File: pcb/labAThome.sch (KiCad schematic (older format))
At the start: 57 parts, among them J1 BME280, J10 SRV2, J12 FA2, J13 Barrel_Jack_Switch, J14 FA3, J2 SRV1, J3 5V, J4 EXTENSION, J5 VPS, J9 FA1, K1 G5V-2, K2 G5V-2, K3 G5V-2, Q2 IRLZ44N, Q3 IRLZ44N, Q4 BC547, SW1 RED, SW2 GREEN, SW3 YELLOW, SW4 BLUE, SW5 WHITE, SW6 FAN, U1 HC-SR501, U2 24V->5V, U3 PDC004_Module, U4 ESP32_DEVKITC_COMPATIBLE, U5 LD06AJSA, U6 GY-302, U7 Display, U8 INMP441_Module

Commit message: SchematicsV3 as ordered at JLCPCB
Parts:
- removed D1: RED, LED_THT:LED_D5.0mm, symbol Device:LED
- removed D2: GREEN, LED_THT:LED_D5.0mm, symbol Device:LED
- removed D3: YELLOW, LED_THT:LED_D5.0mm, symbol Device:LED
- removed J1: BME280, Connector_PinHeader_2.54mm:PinHeader_1x06_P2.54mm_Vertical, symbol Connector:Conn_01x06_Male
- removed J14: FA3, Connector:FanPinHeader_1x03_P2.54mm_Vertical, symbol Connector_Generic:Conn_01x03
- removed J3: 5V, Connector_PinHeader_2.54mm:PinHeader_1x05_P2.54mm_Vertical, symbol Connector_Generic:Conn_01x05
- removed JP3: 3V3_5V, Jumper:SolderJumper-3_P2.0mm_Open_TrianglePad1.0x1.5mm_NumberLabels, symbol Jumper:SolderJumper_3_Open
- removed U1: HC-SR501, smopla:HC-SR501, symbol smopla:HC-SR501
- added C1: CP, Capacitor_THT:CP_Radial_Tantal_D5.0mm_P5.00mm, symbol Device:CP
- added D5: 1N4001, Diode_THT:D_DO-41_SOD81_P7.62mm_Horizontal, symbol Diode:1N4001
- added J1: BME280, Connector_PinHeader_2.54mm:PinHeader_1x04_P2.54mm_Vertical, symbol Connector:Conn_01x04_Male
- added J11, J7, J8: 1wire, Connector_JST:JST_PH_B3B-PH-K_1x03_P2.00mm_Vertical, symbol Connector_Generic:Conn_01x03
- added J3: 5V, Connector_PinHeader_2.54mm:PinHeader_1x04_P2.54mm_Vertical, symbol Connector:Conn_01x04_Male
- added J6: FAN3, Connector:FanPinHeader_1x03_P2.54mm_Vertical, symbol Connector_Generic:Conn_01x03
- added JP3: R3_BUZZ, Connector_PinSocket_2.54mm:PinSocket_1x03_P2.54mm_Vertical, symbol Jumper:Jumper_3_Open
- added JP4: 5V FAN1+2 24V, Connector_PinSocket_2.54mm:PinSocket_1x03_P2.54mm_Vertical, symbol Jumper:Jumper_3_Open
- added Q1: IRLZ44N, Package_TO_SOT_THT:TO-220-3_Horizontal_TabDown, symbol Device:Q_NMOS_GDS
- added U1: SR602, smopla:SR602, symbol smopla:SR602
- added U10: MAX3485_MODULE, smopla:MAX3485_MODULE, symbol smopla:MAX3485_MODULE
- added U11: AM312, smopla:AM312, symbol smopla:HC-SR501
- added U9: NEOPIXEL_STICK, smopla:NEOPIXEL_STICK, symbol smopla:NEOPIXEL_STICK
- added X1: FAN_6024, smopla:FAN_6024, symbol smopla:FAN_6024
- BZ1: footprint Buzzer_Beeper:Buzzer_12x9.5RM7.6 -> smopla:Buzzer_12x9.5RM6.6
- D8: footprint Diode_THT:D_DO-35_SOD27_P7.62mm_Horizontal -> Diode_THT:D_DO-35_SOD27_P2.54mm_Vertical_AnodeUp
- J12: value FA2 -> FAN2
- J9: value FA1 -> FAN1
- Q4: footprint Package_TO_SOT_THT:TO-92_Inline -> Package_TO_SOT_THT:TO-92_HandSolder
- R1, R13, R14, R15, R16, R2, R6: footprint Resistor_THT:R_Axial_DIN0207_L6.3mm_D2.5mm_P7.62mm_Horizontal -> Resistor_THT:R_Axial_DIN0207_L6.3mm_D2.5mm_P2.54mm_Vertical
- R3, R5: value 68R -> 1K; footprint Resistor_THT:R_Axial_DIN0207_L6.3mm_D2.5mm_P7.62mm_Horizontal -> Resistor_THT:R_Axial_DIN0207_L6.3mm_D2.5mm_P2.54mm_Vertical
- R4: value 68R -> 10K; footprint Resistor_THT:R_Axial_DIN0207_L6.3mm_D2.5mm_P7.62mm_Horizontal -> Resistor_THT:R_Axial_DIN0207_L6.3mm_D2.5mm_P2.54mm_Vertical
- SW6: value FAN -> FAN2; footprint smopla:MTS-102 -> smopla:SS12D00
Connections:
- net labels added: 1wire, FAN_SWITCH2, LCD_RES, LED_STRIP
- net labels removed: LED_GREEN, LED_RED, LED_YELLOW
- wire segments 71 -> 80
- no-connect marks 14 -> 16
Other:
- note added: "Gegenseitiger Ausschluss:\n- 1wire und Servo2\n- I2S und RS485\n- Relay 3 und Buzzer"
- note added: "Muss MOSI"
- note added: "PD->Mosfet"
- note added: "PU->SW"
- note removed: "Frei"
- note removed: "PULLED UP"
- note removed: "Soll LED"
- note removed: "Soll SW"
- note removed: "WPD Soll Mosfet"
- moved on the sheet: BZ1, D4, J10, J12, J2, J4, J5, J9, JP2, K1, Q2, Q3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

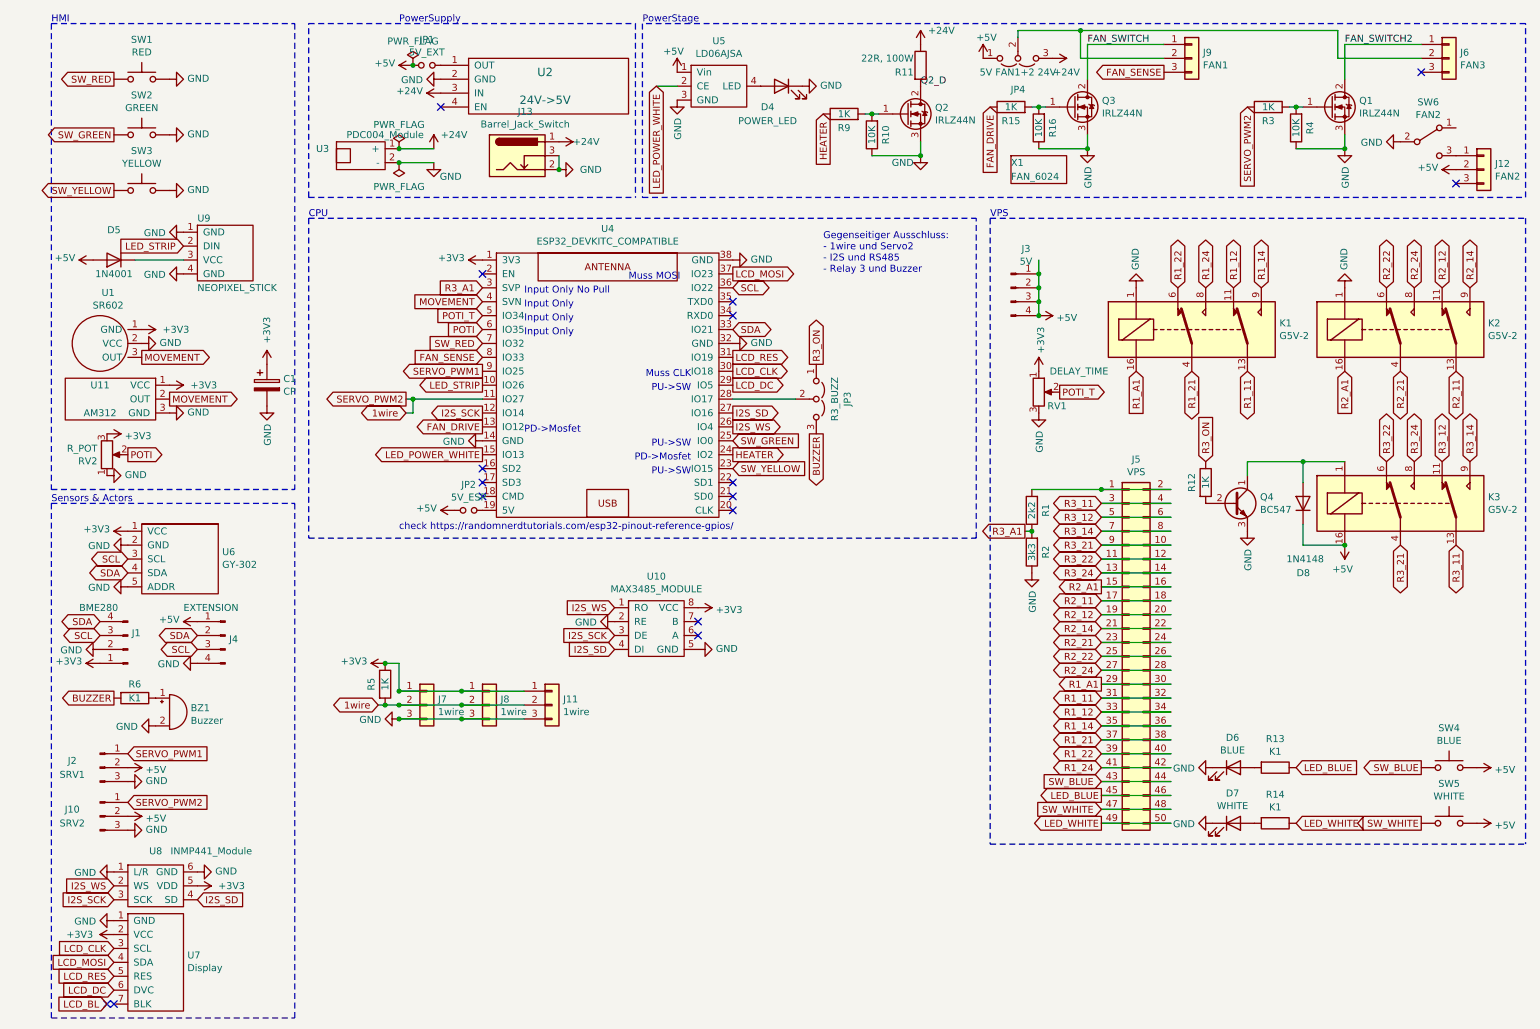
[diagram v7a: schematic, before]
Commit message: PCB  V4 as ordered at JLCPCB
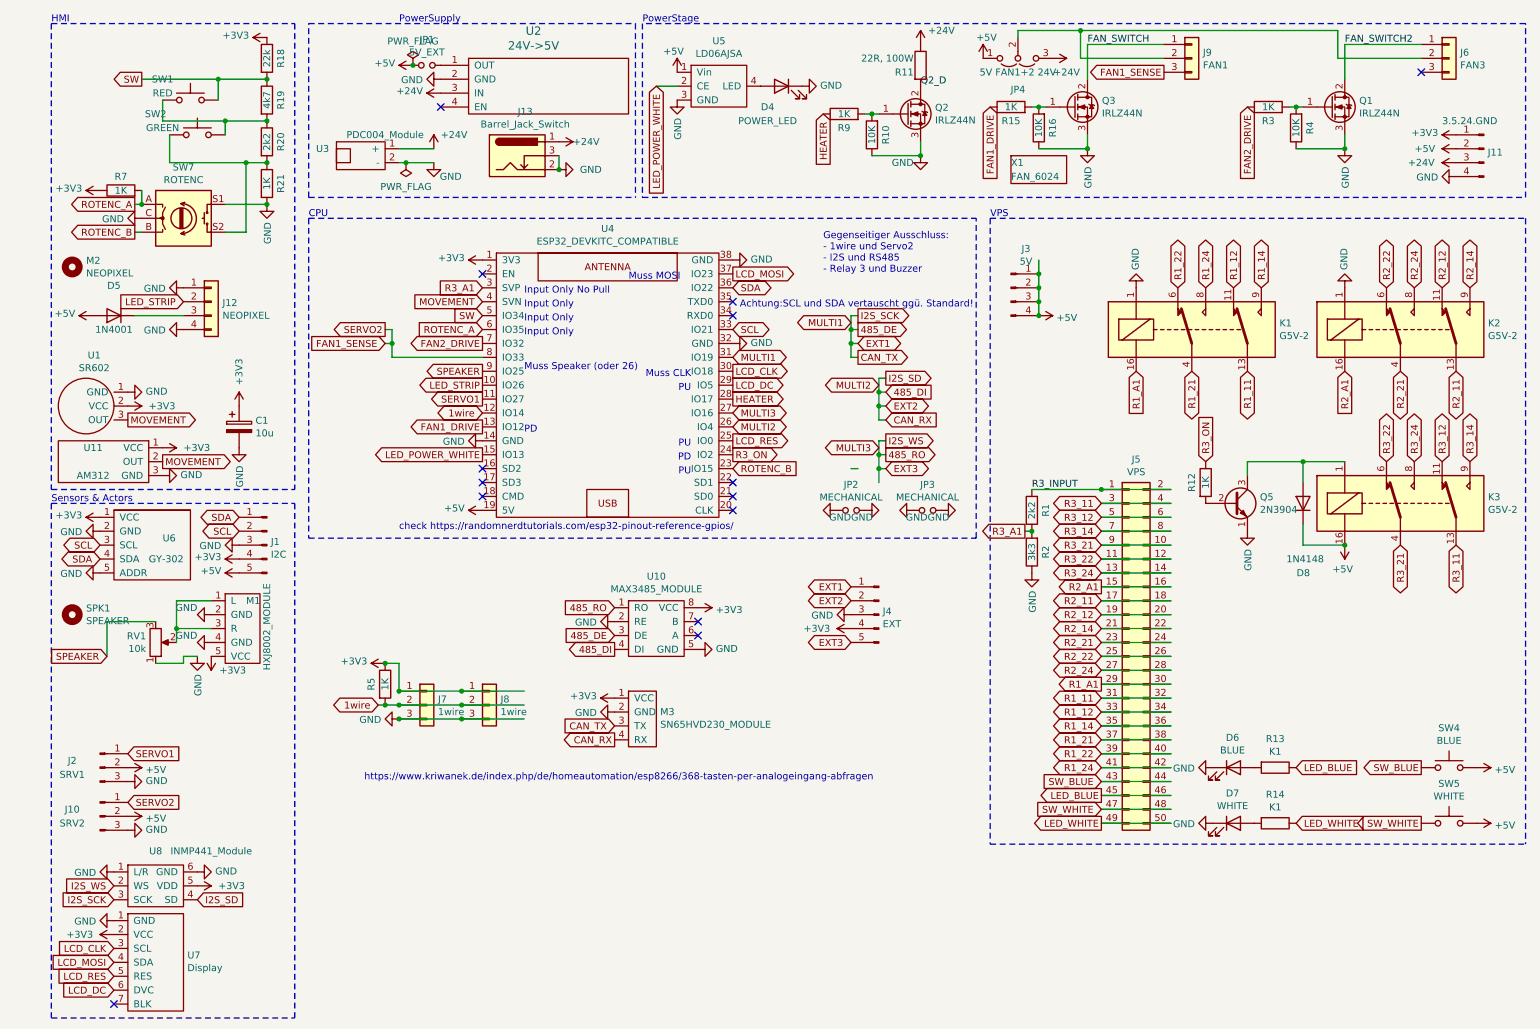
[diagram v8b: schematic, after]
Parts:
- removed BZ1: Buzzer, smopla:Buzzer_12x9.5RM6.6, symbol Device:Buzzer
- removed J1: BME280, Connector_PinHeader_2.54mm:PinHeader_1x04_P2.54mm_Vertical, symbol Connector:Conn_01x04_Male
- removed J11: 1wire, Connector_JST:JST_PH_B3B-PH-K_1x03_P2.00mm_Vertical, symbol Connector_Generic:Conn_01x03
- removed J12: FAN2, Connector:FanPinHeader_1x03_P2.54mm_Vertical, symbol Connector_Generic:Conn_01x03
- removed J4: EXTENSION, Connector_JST:JST_XH_B4B-XH-A_1x04_P2.50mm_Vertical, symbol Connector:Conn_01x04_Male
- removed JP3: R3_BUZZ, Connector_PinSocket_2.54mm:PinSocket_1x03_P2.54mm_Vertical, symbol Jumper:Jumper_3_Open
- removed Q4: BC547, Package_TO_SOT_THT:TO-92_HandSolder, symbol Transistor_BJT:BC547
- removed R6: K1, Resistor_THT:R_Axial_DIN0207_L6.3mm_D2.5mm_P2.54mm_Vertical, symbol Device:R
- removed RV2: R_POT, Potentiometer_THT:Potentiometer_Alpha_RD901F-40-00D_Single_Vertical, symbol Device:R_POT
- removed SW3: YELLOW, Button_Switch_THT:SW_PUSH-12mm, symbol Switch:SW_Push
- removed SW6: FAN2, smopla:SS12D00, symbol Switch:SW_SPDT
- removed U9: NEOPIXEL_STICK, smopla:NEOPIXEL_STICK, symbol smopla:NEOPIXEL_STICK
- added J1: I2C, Connector_JST:JST_XH_B5B-XH-AM_1x05_P2.50mm_Vertical, symbol Connector:Conn_01x05_Male
- added J11: 3.5.24.GND, Connector_JST:JST_XH_B4B-XH-A_1x04_P2.50mm_Vertical, symbol Connector:Conn_01x04_Male
- added J12: NEOPIXEL, Connector_PinSocket_2.54mm:PinSocket_1x04_P2.54mm_Vertical, symbol Connector_Generic:Conn_01x04
- added J4: EXT, Connector_JST:JST_XH_B5B-XH-AM_1x05_P2.50mm_Vertical, symbol Connector:Conn_01x05_Male
- added JP3: MECHANICAL, Connector_PinHeader_2.54mm:PinHeader_1x02_P2.54mm_Vertical, symbol Device:Jumper_NO_Small
- added M1: HXJ8002_MODULE, smopla:HXJ8002_MODULE_VERTICAL, symbol smopla:HXJ8002_MODULE
- added M2: NEOPIXEL, smopla:NEOPIXEL_STICK, symbol Mechanical:MountingHole
- added M3: SN65HVD230_MODULE, smopla:SN65HVD230_MODULE, symbol smopla:SN65HVD230_MODULE
- added Q5: 2N3904, Package_TO_SOT_THT:TO-92_HandSolder, symbol Transistor_BJT:2N3904
- added R18: 22k, Resistor_THT:R_Axial_DIN0207_L6.3mm_D2.5mm_P2.54mm_Vertical, symbol Device:R
- added R19: 4k7, Resistor_THT:R_Axial_DIN0207_L6.3mm_D2.5mm_P2.54mm_Vertical, symbol Device:R
- added R20: 2k2, Resistor_THT:R_Axial_DIN0207_L6.3mm_D2.5mm_P2.54mm_Vertical, symbol Device:R
- added R21, R7: 1K, Resistor_THT:R_Axial_DIN0207_L6.3mm_D2.5mm_P2.54mm_Vertical, symbol Device:R
- added SPK1: SPEAKER, smopla:SPEAKER_2415, symbol Mechanical:MountingHole
- added SW7: ROTENC, smopla:RotaryEncoder_Alps_EC11E-Switch_Vertical_H20mm, symbol Device:Rotary_Encoder_Switch
- C1: value CP -> 10u
- JP2: value 5V_ESP -> MECHANICAL
- R12, R9: footprint Resistor_THT:R_Axial_DIN0207_L6.3mm_D2.5mm_P7.62mm_Horizontal -> Resistor_THT:R_Axial_DIN0207_L6.3mm_D2.5mm_P2.54mm_Vertical
- RV1: value DELAY_TIME -> 10k; footprint Potentiometer_THT:Potentiometer_Bourns_3296W_Vertical -> Potentiometer_THT:Potentiometer_Runtron_RM-065_Vertical
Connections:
- net labels added: 485_DE, 485_DI, 485_RO, CAN_RX, CAN_TX, EXT1, EXT2, EXT3, FAN1_DRIVE, FAN1_SENSE, FAN2_DRIVE, MULTI1, MULTI2, MULTI3, R3_INPUT, ROTENC_A, ROTENC_B, SERVO1, SERVO2, SPEAKER, SW
- net labels removed: BUZZER, FAN_DRIVE, FAN_SENSE, LCD_BL, POTI, POTI_T, SERVO_PWM1, SERVO_PWM2, SW_GREEN, SW_RED, SW_YELLOW
- wire segments 80 -> 127
- no-connect marks 16 -> 14
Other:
- note added: "Achtung:SCL und SDA vertauscht ggü. Standard!"
- note added: "Muss Speaker (oder 26)"
- note added: "PD"
- note added: "PU"
- note added: "https://www.kriwanek.de/index.php/de/homeautomation/esp8266/368-tasten-per-analogeingang-abfragen"
- note removed: "PD->Mosfet"
- note removed: "PU->SW"
- moved on the sheet: C1, D5, SW1, SW2, U1, U11, U6
